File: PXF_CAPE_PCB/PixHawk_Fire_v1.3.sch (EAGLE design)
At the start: 242 parts, among them J305 DF13-3P-1.25V, J306 DF13-4P-1.25V, J307 DF13-4P-1.25V, J308 DF13-4P-1.25V, J309 DF13-5P-1.25V, J310 DF13-4P-1.25V, J314 DF13-4P-1.25V, J701 JST-ZH-3, J801 DF13C-6P-1.25V, M3_MOUNT901 MOUNT-HOLE3.1MM, M3_MOUNT902 MOUNT-HOLE3.1MM, M3_MOUNT903 MOUNT-HOLE3.1MM, M3_MOUNT904 MOUNT-HOLE3.1MM, Q501 MMBT3906LT1SMD, U1 EEPROM-I2CSMD, U102 FM25V01, U2 EEPROM-I2CSMD, U201 TXS0108QFN20, U202 TXS0108QFN20, U301 MAX3051, U302 TXS0108QFN20, U303 PCA9306, U401 MS5611-01BA, U402 MS5611-01BA, U403 MPU-6000, U405 MPU-9250, U406 LSM9DS0LSM9DS0, U407 BMP280_PRELIM, U501 BQ24315, U502 MIC5332, U503 BQ24315, U601 TCA62724FMG, U602 LT3469, U603 LRTB GFTG-T7AW-1+V7A7-29+R5T9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, U701 TXS0108QFN20, U702 TXS0108QFN20, U703 74LVC2G240, U704 BBB_3X14_RA, U801 BQ24313, U802 MIC5332, X801 4 pin head

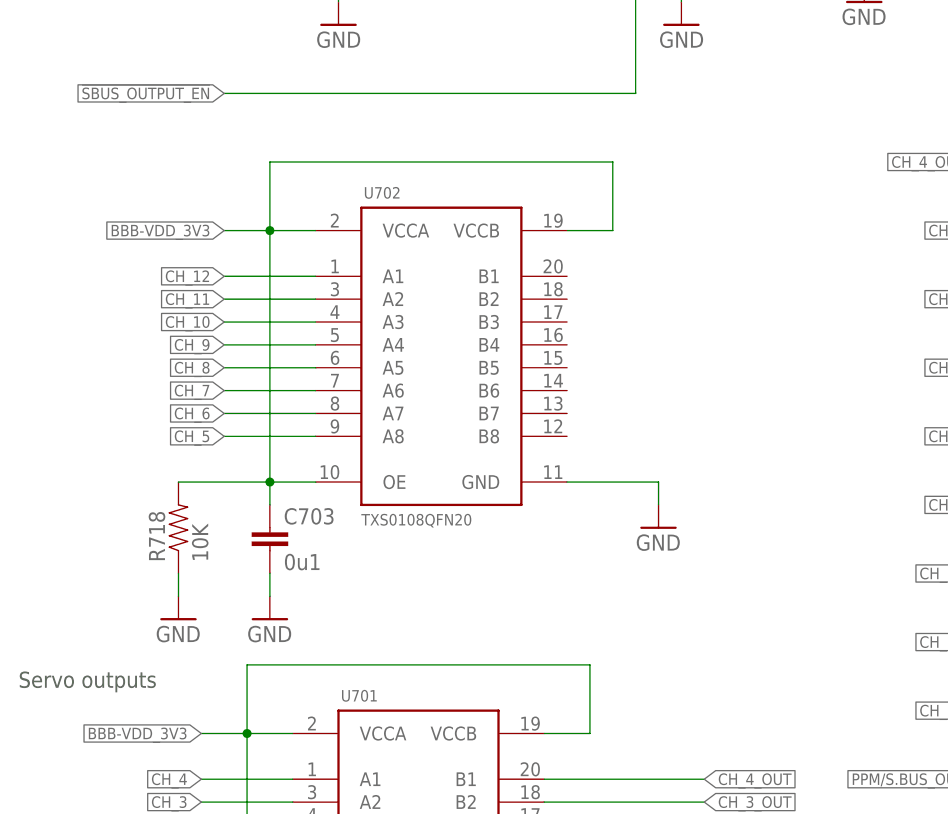
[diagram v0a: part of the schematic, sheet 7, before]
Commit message: ISSUE#3 v2: Removal of the Voltage Trns. U702
Removal of U702, R718 and C703. Retracing of this area. Notice there is
a airwire in point 3880,929.5. I have tried to remove it with little
success.
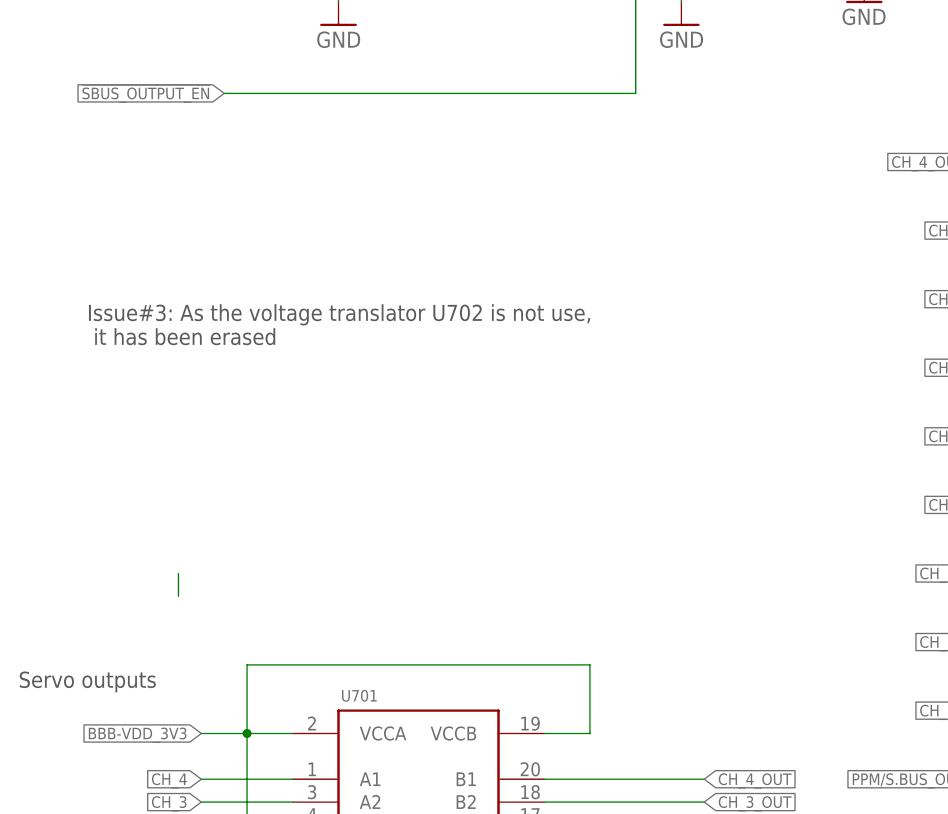
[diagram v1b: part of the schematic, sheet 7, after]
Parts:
- removed C703: 0u1, pixhawk2:CAP0402
- removed R718: 10K, pixhawk2:RESISTOR0402-RES
- removed U702: TXS0108QFN20, pixhawk2:TXS0108QFN20
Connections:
- net BBB-VDD_3V3: no longer C703.1, R718.2, U702.OE, U702.VCCA, U702.VCCB
- net CH_10: no longer U702.A3
- net CH_11: no longer U702.A2
- net CH_12: no longer U702.A1
- net CH_5: no longer U702.A8
- net CH_6: no longer U702.A7
- net CH_7: no longer U702.A6
- net CH_8: no longer U702.A5
- net CH_9: no longer U702.A4
- net GND: no longer C703.2, R718.1, U702.GND
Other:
- note added: "Issue#3: As the voltage translator U702 is not use, it has been erased"
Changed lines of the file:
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@@
 <attribute name="PARTNO" value="LRTB GFTG-T7AW-1+V7A7-29+R5T9-49-L"/>
 </part>
-<part name="C703" library="pixhawk2" deviceset="CAP" device="0402" value="0u1">
-<attribute name="PARTNO" value="CC0402ZRY5V7BB104"/>
-</part>
-<part name="GND18" library="pixhawk2" deviceset="GND" device=""/>
 <part name="U602" library="pixhawk2" deviceset="LT3469" device="" value="LT3469">
 <attribute name="PARTNO" value="LT3469ETS8"/>
@@
 <attribute name="PARTNO" value="TXS0108ERGYR"/>
 </part>
-<part name="U702" library="pixhawk2" deviceset="TXS0108" device="QFN20">
-<attribute name="PARTNO" value="TXS0108ERGYR"/>
-</part>
 <part name="U703" library="pixhawk2" deviceset="74LVC2G240" device="-TSSOP-8" value="74LVC2G240">
 <attribute name="PARTNO" value="74LVC2G240DP,125"/>
@@
 <attribute name="PARTNO" value="ERA-2AEB103X"/>
 </part>
-<part name="GND60" library="pixhawk2" deviceset="GND" device=""/>
-<part name="R718" library="pixhawk2" deviceset="RESISTOR" device="0402-RES" value="10K">
-<attribute name="PARTNO" value="ERA-2AEB103X"/>
-</part>
 <part name="R719" library="pixhawk2" deviceset="RESISTOR" device="0402-RES" value="10K">
 <attribute name="PARTNO" value="ERA-2AEB103X"/>
 </part>
-<part name="GND62" library="pixhawk2" deviceset="GND" device=""/>
 <part name="GND70" library="pixhawk2" deviceset="GND" device=""/>
 <part name="GND73" library="pixhawk2" deviceset="GND" device=""/>
@@
 for use in a flying vehicle, ensure that you have complied with any requirements found on Ardupilot.com in preparing the Certificate of Authenticity that will reside on the SHA chip on the board.
 if you make a clone or derivative of this board, you must release your exact schematics and PCB doccuments, and include these notices on every page.</text>
+<text x="15.24" y="96.52" size="1.778" layer="97">Issue#3: As the voltage translator U702 is not use,
+ it has been erased</text>
 </plain>
 <instances>
@@
 <attribute name="PARTNO" x="33.02" y="17.78" size="1.778" layer="96" display="off"/>
 </instance>
-<instance part="C703" gate="G$1" x="35.56" y="73.66">
-<attribute name="PARTNO" x="35.56" y="73.66" size="1.778" layer="96" display="off"/>
-</instance>
-<instance part="GND18" gate="1" x="78.74" y="76.2"/>
 <instance part="U701" gate="G$1" x="53.34" y="48.26">
 <attribute name="PARTNO" x="53.34" y="48.26" size="1.778" layer="96" display="off"/>
 </instance>
-<instance part="U702" gate="G$1" x="55.88" y="104.14">
-<attribute name="PARTNO" x="55.88" y="104.14" size="1.778" layer="96" display="off"/>
-</instance>
 <instance part="U703" gate="G$1" x="58.42" y="149.86">
 <attribute name="PARTNO" x="58.42" y="149.86" size="1.778" layer="96" display="off"/>
@@
 <attribute name="PARTNO" x="187.96" y="162.56" size="1.778" layer="96" display="off"/>
 </instance>
-<instance part="GND60" gate="1" x="35.56" y="66.04"/>
-<instance part="R718" gate="G$1" x="25.4" y="76.2" rot="R90">
-<attribute name="PARTNO" x="25.4" y="76.2" size="1.778" layer="96" rot="R90" display="off"/>
-</instance>
 <instance part="R719" gate="G$1" x="22.86" y="20.32" rot="R90">
 <attribute name="PARTNO" x="22.86" y="20.32" size="1.778" layer="96" rot="R90" display="off"/>
 </instance>
-<instance part="GND62" gate="1" x="25.4" y="66.04"/>
 <instance part="GND70" gate="1" x="22.86" y="10.16"/>
 <instance part="GND73" gate="1" x="33.02" y="10.16"/>
@@
 </segment>
 <segment>
-<pinref part="GND18" gate="1" pin="GND"/>
-<pinref part="U702" gate="G$1" pin="GND"/>
-<wire x1="78.74" y1="81.28" x2="78.74" y2="78.74" width="0.1524" layer="91"/>
-<wire x1="68.58" y1="81.28" x2="78.74" y2="81.28" width="0.1524" layer="91"/>
-</segment>
-<segment>
 <pinref part="GND34" gate="1" pin="GND"/>
 <wire x1="76.2" y1="22.86" x2="76.2" y2="25.4" width="0.1524" layer="91"/>
@@
 </segment>
 <segment>
-<pinref part="R718" gate="G$1" pin="1"/>
-<pinref part="GND62" gate="1" pin="GND"/>
-<wire x1="25.4" y1="71.12" x2="25.4" y2="68.58" width="0.1524" layer="91"/>
-</segment>
-<segment>
 <pinref part="R719" gate="G$1" pin="1"/>
 <pinref part="GND70" gate="1" pin="GND"/>
@@
 <wire x1="33.02" y1="15.24" x2="33.02" y2="12.7" width="0.1524" layer="91"/>
 </segment>
-<segment>
-<pinref part="C703" gate="G$1" pin="2"/>
-<pinref part="GND60" gate="1" pin="GND"/>
-<wire x1="35.56" y1="71.12" x2="35.56" y2="68.58" width="0.1524" layer="91"/>
-</segment>
 </net>
 <net name="BBB-VDD_3V3" class="1">
@@
 </segment>
 <segment>
-<label x="30.48" y="109.22" size="1.27" layer="95" rot="R180" xref="yes"/>
-<pinref part="U702" gate="G$1" pin="VCCA"/>
-<wire x1="40.64" y1="109.22" x2="35.56" y2="109.22" width="0.1524" layer="91"/>
-<wire x1="35.56" y1="109.22" x2="30.48" y2="109.22" width="0.1524" layer="91"/>
-<wire x1="35.56" y1="109.22" x2="35.56" y2="116.84" width="0.1524" layer="91"/>
-<pinref part="C703" gate="G$1" pin="1"/>
-<wire x1="35.56" y1="116.84" x2="73.66" y2="116.84" width="0.1524" layer="91"/>
-<pinref part="U702" gate="G$1" pin="VCCB"/>
-<wire x1="68.58" y1="109.22" x2="73.66" y2="109.22" width="0.1524" layer="91"/>
-<wire x1="73.66" y1="109.22" x2="73.66" y2="116.84" width="0.1524" layer="91"/>
-<pinref part="U702" gate="G$1" pin="OE"/>
-<wire x1="40.64" y1="81.28" x2="35.56" y2="81.28" width="0.1524" layer="91"/>
-<wire x1="35.56" y1="81.28" x2="35.56" y2="109.22" width="0.1524" layer="91"/>
-<junction x="35.56" y="109.22"/>
-<wire x1="35.56" y1="78.74" x2="35.56" y2="81.28" width="0.1524" layer="91"/>
-<wire x1="35.56" y1="81.28" x2="25.4" y2="81.28" width="0.1524" layer="91"/>
-<junction x="35.56" y="81.28"/>
-<pinref part="R718" gate="G$1" pin="2"/>
-</segment>
-<segment>
 <wire x1="45.72" y1="157.48" x2="33.02" y2="157.48" width="0.1524" layer="91"/>
 <label x="30.48" y="157.48" size="1.27" layer="95" rot="MR0" xref="yes"/>
@@
 <net name="CH_12" class="0">
 <segment>
-<label x="30.48" y="104.14" size="1.27" layer="95" rot="R180" xref="yes"/>
-<wire x1="30.48" y1="104.14" x2="40.64" y2="104.14" width="0.1524" layer="91"/>
-<pinref part="U702" gate="G$1" pin="A1"/>
-</segment>
-<segment>
 <pinref part="R709" gate="G$1" pin="1"/>
 <wire x1="119.38" y1="55.88" x2="114.3" y2="55.88" width="0.1524" layer="91"/>
@@
 <net name="CH_11" class="0">
 <segment>
-<label x="30.48" y="101.6" size="1.27" layer="95" rot="R180" xref="yes"/>
-<wire x1="30.48" y1="101.6" x2="40.64" y2="101.6" width="0.1524" layer="91"/>
-<pinref part="U702" gate="G$1" pin="A2"/>
-</segment>
-<segment>
 <pinref part="R708" gate="G$1" pin="1"/>
 <wire x1="119.38" y1="63.5" x2="114.3" y2="63.5" width="0.1524" layer="91"/>
@@
 <net name="CH_10" class="0">
 <segment>
-<label x="30.48" y="99.06" size="1.27" layer="95" rot="R180" xref="yes"/>
-<pinref part="U702" gate="G$1" pin="A3"/>
-<wire x1="30.48" y1="99.06" x2="40.64" y2="99.06" width="0.1524" layer="91"/>
-</segment>
-<segment>
 <pinref part="R707" gate="G$1" pin="1"/>
 <wire x1="119.38" y1="71.12" x2="114.3" y2="71.12" width="0.1524" layer="91"/>
@@
 <net name="CH_7" class="0">
 <segment>
-<label x="30.48" y="91.44" size="1.27" layer="95" rot="R180" xref="yes"/>
-<wire x1="30.48" y1="91.44" x2="40.64" y2="91.44" width="0.1524" layer="91"/>
-<pinref part="U702" gate="G$1" pin="A6"/>
-</segment>
-<segment>
 <pinref part="R704" gate="G$1" pin="1"/>
 <wire x1="119.38" y1="93.98" x2="114.3" y2="93.98" width="0.1524" layer="91"/>
@@
 <net name="CH_6" class="0">
 <segment>
-<label x="30.48" y="88.9" size="1.27" layer="95" rot="R180" xref="yes"/>
-<pinref part="U702" gate="G$1" pin="A7"/>
-<wire x1="40.64" y1="88.9" x2="30.48" y2="88.9" width="0.1524" layer="91"/>
-</segment>
-<segment>
 <pinref part="R703" gate="G$1" pin="1"/>
 <wire x1="119.38" y1="101.6" x2="114.3" y2="101.6" width="0.1524" layer="91"/>
@@
 <net name="CH_5" class="0">
 <segment>
-<label x="30.48" y="86.36" size="1.27" layer="95" rot="R180" xref="yes"/>
-<pinref part="U702" gate="G$1" pin="A8"/>
-<wire x1="30.48" y1="86.36" x2="40.64" y2="86.36" width="0.1524" layer="91"/>
-</segment>
-<segment>
 <pinref part="R702" gate="G$1" pin="1"/>
 <wire x1="119.38" y1="109.22" x2="114.3" y2="109.22" width="0.1524" layer="91"/>
@@
 <net name="CH_9" class="0">
 <segment>
-<pinref part="U702" gate="G$1" pin="A4"/>
-<wire x1="40.64" y1="96.52" x2="30.48" y2="96.52" width="0.1524" layer="91"/>
-<label x="30.48" y="96.52" size="1.27" layer="95" rot="R180" xref="yes"/>
-</segment>
-<segment>
 <pinref part="R706" gate="G$1" pin="1"/>
 <wire x1="119.38" y1="78.74" x2="114.3" y2="78.74" width="0.1524" layer="91"/>
@@
 <net name="CH_8" class="0">
 <segment>
-<pinref part="U702" gate="G$1" pin="A5"/>
-<wire x1="40.64" y1="93.98" x2="30.48" y2="93.98" width="0.1524" layer="91"/>
-<label x="30.48" y="93.98" size="1.27" layer="95" rot="R180" xref="yes"/>
-</segment>
-<segment>
 <pinref part="R705" gate="G$1" pin="1"/>
 <wire x1="119.38" y1="86.36" x2="114.3" y2="86.36" width="0.1524" layer="91"/>
@@
 </segment>
 </net>
+<net name="N$62" class="1">
+<segment>
+<wire x1="25.4" y1="71.12" x2="25.4" y2="68.58" width="0.1524" layer="91"/>
+</segment>
+</net>

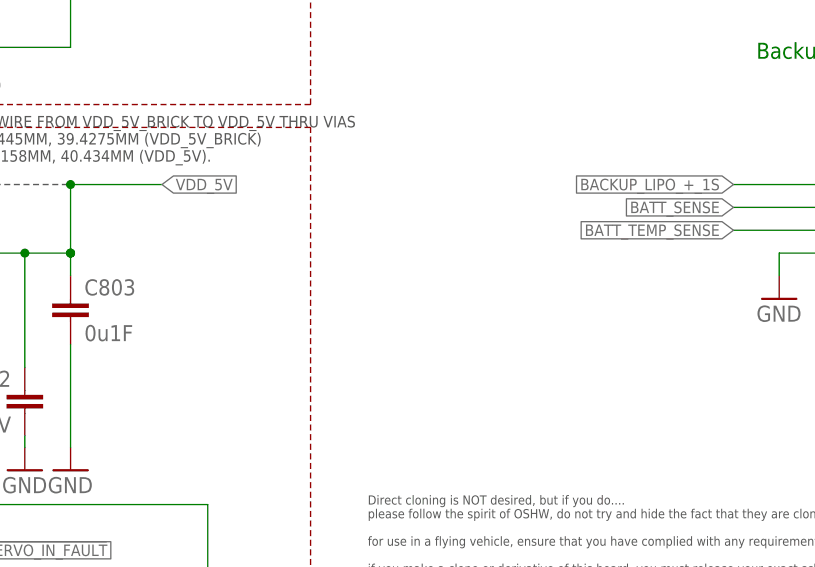
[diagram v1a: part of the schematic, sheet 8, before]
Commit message: Address issue #2.
This fix avoid having to hand solder a cable
between VDD_5V and VDD_5V_BRICK. The fix
allows to use the Power Module to power the
board directly.
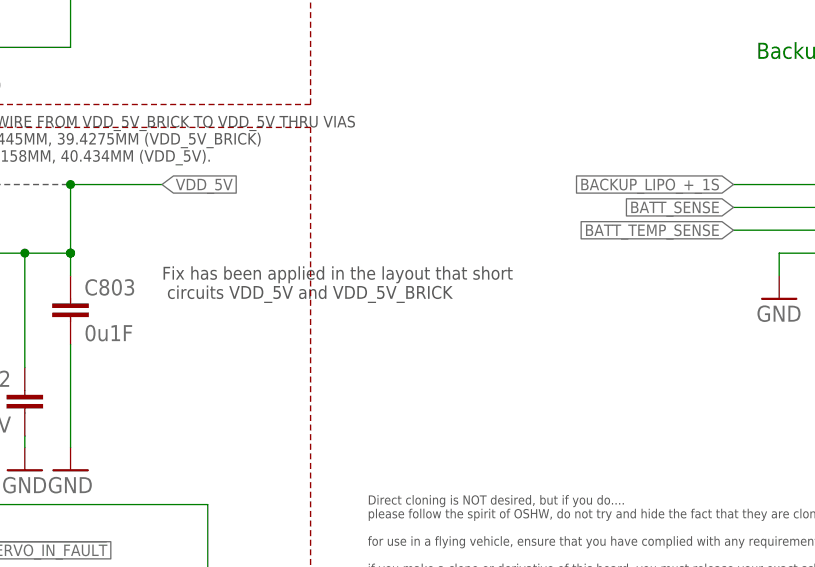
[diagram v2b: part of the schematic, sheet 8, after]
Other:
- note added: "Fix has been applied in the layout that short circuits VDD_5V and VDD_5V_BRICK"
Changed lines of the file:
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@@
 <?xml version="1.0" encoding="utf-8"?>
 <!DOCTYPE eagle SYSTEM "eagle.dtd">
-<eagle version="6.6.0">
+<eagle version="6.4">
 <drawing>
 <settings>
@@
 for use in a flying vehicle, ensure that you have complied with any requirements found on Ardupilot.com in preparing the Certificate of Authenticity that will reside on the SHA chip on the board.
 if you make a clone or derivative of this board, you must release your exact schematics and PCB doccuments, and include these notices on every page.</text>
+<text x="96.52" y="71.12" size="1.4224" layer="97">Fix has been applied in the layout that short
+ circuits VDD_5V and VDD_5V_BRICK</text>
 </plain>
 <instances>
